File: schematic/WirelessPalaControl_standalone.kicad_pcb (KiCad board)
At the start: 2 copper layers, 25.6 x 34.3 mm, 25 parts, among them J1 6P4C, J2 MCU UART, J3 WeMos_mini_Hat_Left, J4 WeMos_mini_Hat_Right, Q1 AO3400A, Q2 AO3400A, U1 AMS1117-3.3

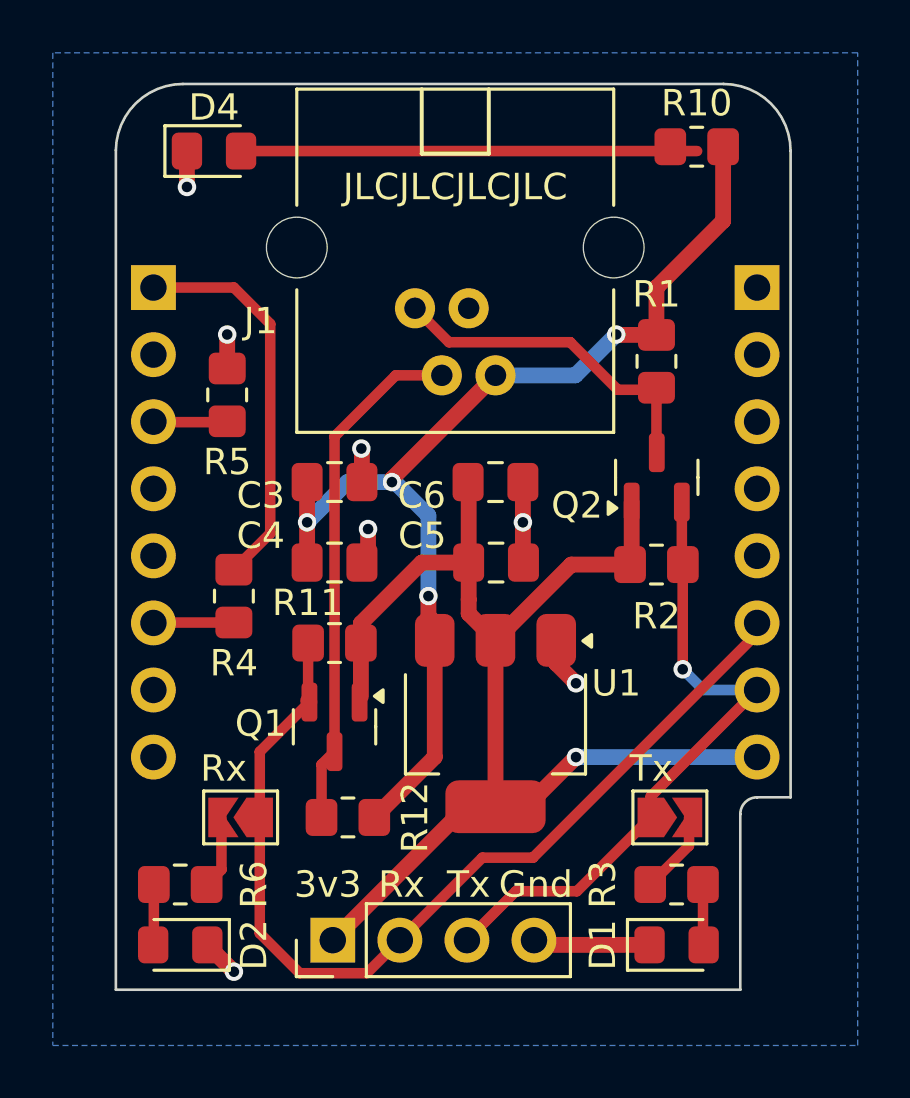
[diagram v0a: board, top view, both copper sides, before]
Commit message: feat(hw): Redesign standalone version with optionnal LED activation
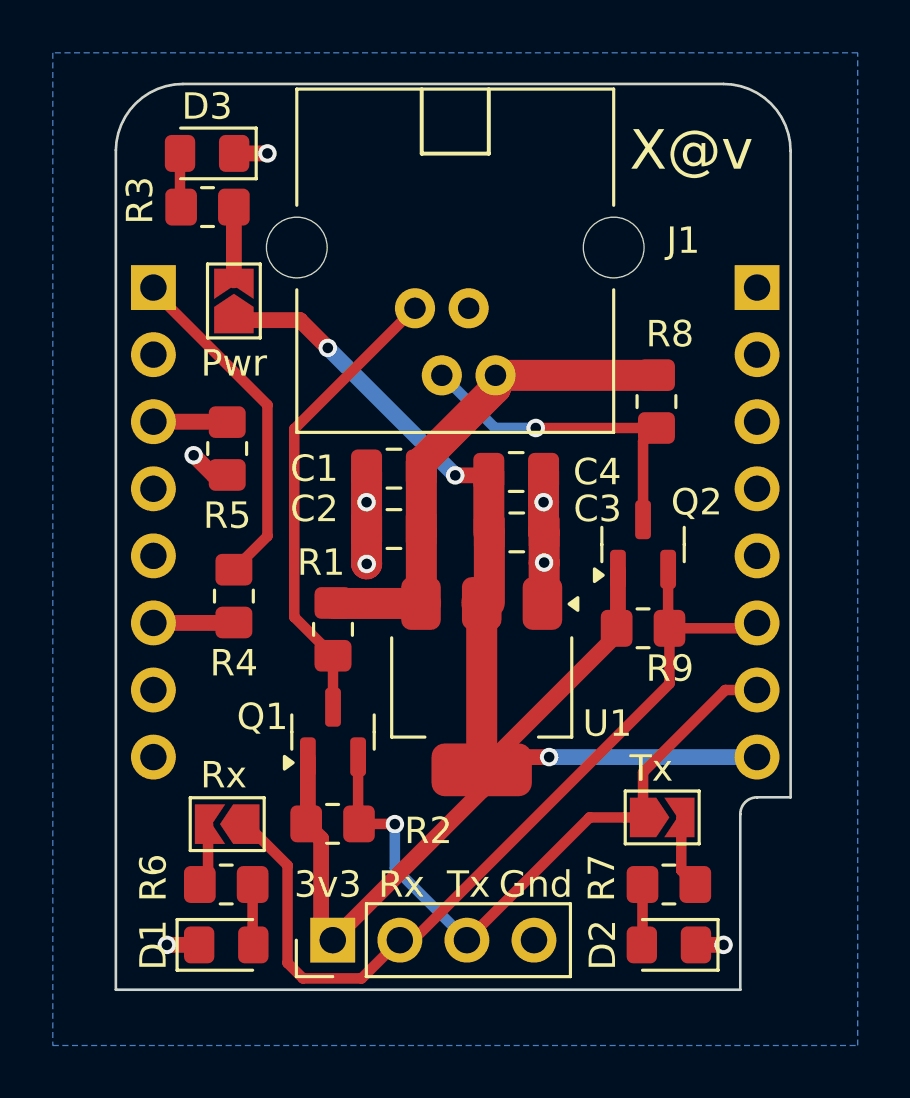
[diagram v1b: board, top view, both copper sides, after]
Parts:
- added JP3: SolderJumper_2_Open, Jumper:SolderJumper-2_P1.3mm_Open_TrianglePad1.0x1.5mm, F.Cu at (27.2, 32.3)
- moved R8 19.6 mm to (43.2, 36.1), turned to 90 degrees
- moved R3 18.7 mm to (26.2, 28.7)
- moved R1 15.9 mm to (30.9, 44.7)
- moved R2 15.7 mm to (30.9, 52.1)
- moved Q1 15.6 mm to (30.9, 48.6)
- moved Q2 13.6 mm to (42.7, 41.5), turned to 90 degrees
- moved R9 11.7 mm to (42.7, 44.7), turned to 180 degrees
- moved C2 2.58 mm to (33.2, 40.9), turned to 180 degrees
- moved C1 2.31 mm to (33.2, 38.6), turned to 180 degrees
- moved R5 2.03 mm to (26.9, 37.8), turned to -90 degrees
- moved D1 1.74 mm to (26.9, 56.6), turned to 0 degrees
- moved R6 1.74 mm to (26.9, 54.4), turned to 180 degrees
- moved U1 1.49 mm to (36.6, 46.9)
- moved C3 1.39 mm to (37.9, 41.0)
- moved C4 0.87 mm to (37.9, 38.7)
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- renumbered C3 to C1, C4 to C2, C5 to C3, C6 to C4, D2 to D1, D1 to D2, D4 to D3, Q2 to Q1, Q1 to Q2, R10 to R3, R3 to R7, R12 to R8, R11 to R9
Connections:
- R3 pad 2: +5V -> Net-(JP3-B)
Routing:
- net +5V: track 41.4 -> 19.3 mm, vias 4 -> 0
- net Net-(D3-A): track 17.3 -> 2.05 mm
- net +3.3V: track 48.7 -> 59.7 mm, vias 1 -> 3
- net Rx: track 19.7 -> 12.6 mm, vias 0 -> 1
- net Tx: track 12.9 -> 17.6 mm
- net RXuC: track 37.0 -> 33.0 mm
- net GND: track 16.8 -> 13.5 mm, vias 7 -> 8
- net Net-(JP3-B): track 0.00 -> 2.78 mm
- net /GPIO1: track 14.9 -> 13.0 mm
- net TXuC: track 24.9 -> 25.8 mm
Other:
- board text added: "Domochip WPalaControl V3.1"
- board text added: "Pwr"
- board text added: "X@v"
- board text removed: "Domochip WPalaControl V3.0"

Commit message: feat(hw): Add connector to directly solder a RJ11 cable
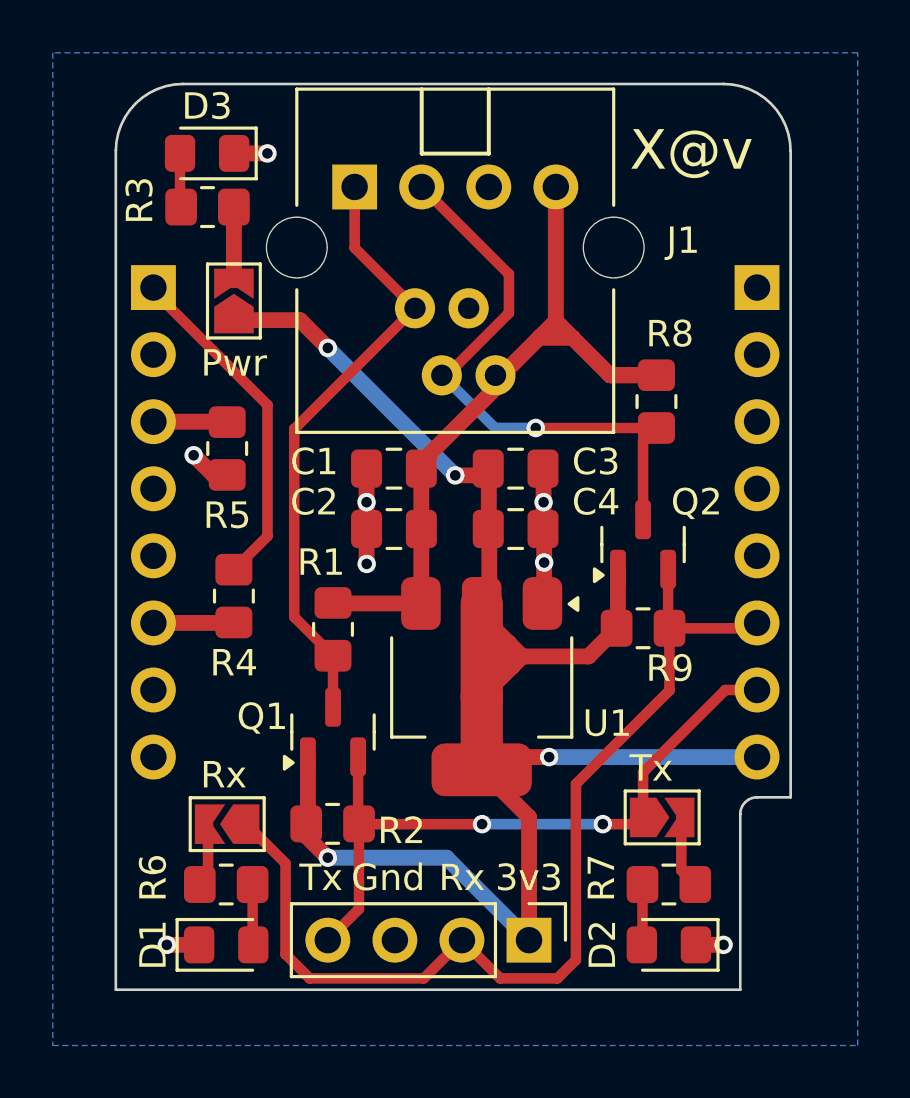
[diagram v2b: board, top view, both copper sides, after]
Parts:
- added J5: RJ11 - Direct Link, Connector_PinHeader_2.54mm:PinHeader_1x04_P2.54mm_Vertical, B.Cu at (31.8, 27.9)
- R1, R2, R8, R9: value 1K -> 10K
- moved J2 7.43 mm to (38.4, 56.5), turned to -90 degrees
- moved C3 2.41 mm to (37.8, 38.6)
- moved C4 2.16 mm to (37.8, 40.9)
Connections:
- J2 pad 3: TXuC -> GND
- J2 pad 4: GND -> TXuC
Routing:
- net +5V: track 19.3 -> 29.1 mm
- net Rx: track 12.6 -> 22.3 mm
- net +3.3V: track 59.7 -> 66.4 mm, vias 3 -> 4
- net Tx: track 17.6 -> 23.2 mm
- net RXuC: track 33.0 -> 38.1 mm
- net TXuC: vias 1 -> 2
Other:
- board text added: "RJ11 Y G R Bk colors"

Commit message: feat(hw): Update BOM with JLCPCB part numbers
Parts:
- R4: value 2K -> 1K
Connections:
- R4 pad 1: /GPIO1 -> /GPIO2
- R4 pad 2: /GPIO2 -> /GPIO1
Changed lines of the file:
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@@
 			)
 		)
-		(property "LCSC" "C17513"
+		(property "LCSC" "C17414"
 			(at 0 0 180)
 			(unlocked yes)
@@
 			)
 		)
-		(property "LCSC" "C17513"
+		(property "LCSC" "C17414"
 			(at 0 0 90)
 			(unlocked yes)
@@
 			)
 		)
-		(property "LCSC" "C84256"
+		(property "LCSC" "C2297"
 			(at 0 0 0)
 			(unlocked yes)
@@
 			)
 		)
-		(property "Value" "2K"
+		(property "Value" "1K"
 			(at 0 1.65 90)
 			(layer "F.Fab")
@@
 			)
 		)
-		(property "LCSC" "C17604"
+		(property "LCSC" "C17513"
 			(at 0 0 270)
 			(unlocked yes)
@@
 			(layers "F.Cu" "F.Mask" "F.Paste")
 			(roundrect_rratio 0.208333)
-			(net 8 "/GPIO1")
+			(net 12 "/GPIO2")
 			(pintype "passive")
 		)
@@
 			(layers "F.Cu" "F.Mask" "F.Paste")
 			(roundrect_rratio 0.208333)
-			(net 12 "/GPIO2")
+			(net 8 "/GPIO1")
 			(pintype "passive")
 		)
@@
 			)
 		)
-		(property "LCSC" "C17513"
+		(property "LCSC" "C17414"
 			(at 0 0 180)
 			(unlocked yes)
@@
 			)
 		)
-		(property "LCSC" "C17513"
+		(property "LCSC" "C17414"
 			(at 0 0 90)
 			(unlocked yes)
@@
 		(sheetname "/")
 		(sheetfile "WirelessPalaControl_standalone.kicad_sch")
-		(attr through_hole exclude_from_pos_files)
+		(attr through_hole exclude_from_pos_files exclude_from_bom)
 		(fp_line
 			(start 1.33 1.33)
@@
 		(sheetname "/")
 		(sheetfile "WirelessPalaControl_standalone.kicad_sch")
-		(attr through_hole exclude_from_pos_files)
+		(attr through_hole exclude_from_pos_files exclude_from_bom)
 		(fp_line
 			(start 1.33 -1.27)

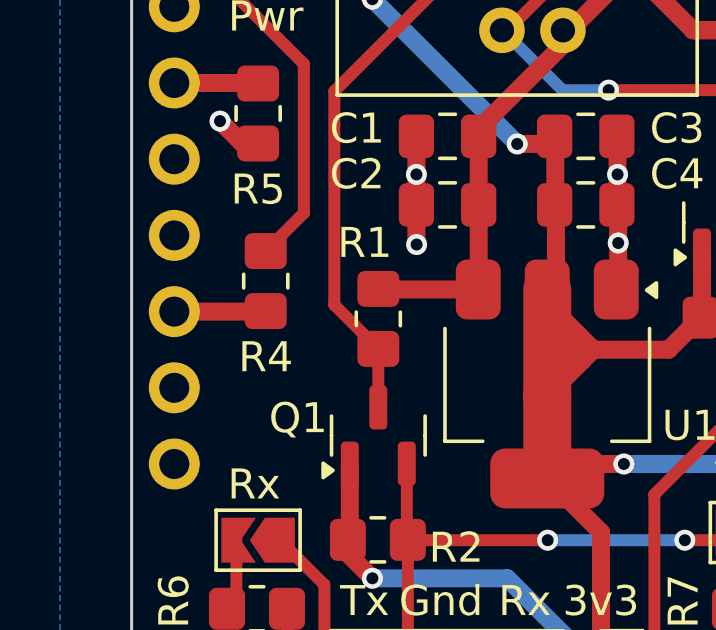
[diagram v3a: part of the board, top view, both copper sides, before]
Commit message: feat(hw): Cleanup schematic
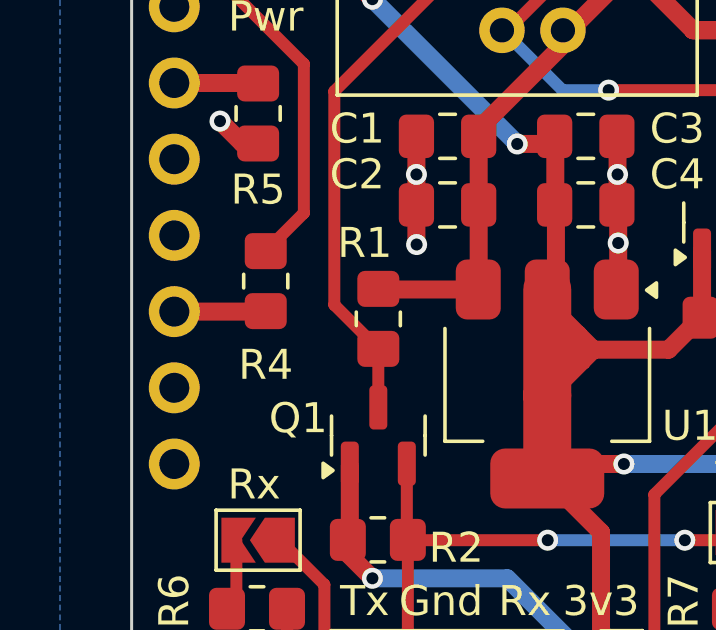
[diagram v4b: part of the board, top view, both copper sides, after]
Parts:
- turned R4 to 90 degrees
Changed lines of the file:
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@@
 	(footprint "Resistor_SMD:R_0805_2012Metric_Pad1.20x1.40mm_HandSolder"
 		(layer "F.Cu")
-		(at 27.178 43.434 -90)
+		(at 27.178 43.434 90)
 		(descr "Resistor SMD 0805 (2012 Metric), square (rectangular) end terminal, IPC_7351 nominal with elongated pad for handsoldering. (Body size source: IPC-SM-782 page 72, https://www.pcb-3d.com/wordpress/wp-content/uploads/ipc-sm-782a_amendment_1_and_2.pdf), generated with kicad-footprint-generator")
 		(tags "resistor handsolder")
 		(property "Reference" "R4"
-			(at 2.54 0 180)
+			(at -2.794 0 0)
 			(layer "F.SilkS")
 			(effects
@@
 		)
 		(property "Datasheet" "~"
-			(at 0 0 270)
+			(at 0 0 90)
 			(unlocked yes)
 			(layer "F.Fab")
@@
 		)
 		(property "Description" ""
-			(at 0 0 270)
+			(at 0 0 90)
 			(unlocked yes)
 			(layer "F.Fab")
@@
 		)
 		(property "LCSC" "C17513"
-			(at 0 0 270)
+			(at 0 0 90)
 			(unlocked yes)
 			(layer "F.Fab")
@@
 		(attr smd)
 		(fp_line
+			(start -0.227064 -0.735)
+			(end 0.227064 -0.735)
+			(stroke
+				(width 0.12)
+				(type solid)
+			)
+			(layer "F.SilkS")
+		)
+		(fp_line
 			(start -0.227064 0.735)
 			(end 0.227064 0.735)
@@
 		)
 		(fp_line
-			(start -0.227064 -0.735)
-			(end 0.227064 -0.735)
+			(start 1.85 -0.95)
+			(end 1.85 0.95)
 			(stroke
-				(width 0.12)
+				(width 0.05)
 				(type solid)
 			)
-			(layer "F.SilkS")
+			(layer "F.CrtYd")
 		)
 		(fp_line
-			(start -1.85 0.95)
-			(end -1.85 -0.95)
+			(start -1.85 -0.95)
+			(end 1.85 -0.95)
 			(stroke
 				(width 0.05)
@@
 		)
 		(fp_line
-			(start -1.85 -0.95)
-			(end 1.85 -0.95)
+			(start -1.85 0.95)
+			(end -1.85 -0.95)
 			(stroke
 				(width 0.05)
@@
 		)
 		(fp_line
-			(start 1.85 -0.95)
-			(end 1.85 0.95)
+			(start 1 -0.625)
+			(end 1 0.625)
 			(stroke
-				(width 0.05)
+				(width 0.1)
 				(type solid)
 			)
-			(layer "F.CrtYd")
+			(layer "F.Fab")
 		)
 		(fp_line
-			(start -1 0.625)
-			(end -1 -0.625)
+			(start -1 -0.625)
+			(end 1 -0.625)
 			(stroke
 				(width 0.1)
@@
 		)
 		(fp_line
-			(start -1 -0.625)
-			(end 1 -0.625)
-			(stroke
-				(width 0.1)
-				(type solid)
-			)
-			(layer "F.Fab")
-		)
-		(fp_line
-			(start 1 -0.625)
-			(end 1 0.625)
+			(start -1 0.625)
+			(end -1 -0.625)
 			(stroke
 				(width 0.1)
@@
 		)
 		(pad "1" smd roundrect
-			(at -1 0 270)
+			(at -1 0 90)
 			(size 1.2 1.4)
 			(layers "F.Cu" "F.Mask" "F.Paste")
@@
 		)
 		(pad "2" smd roundrect
-			(at 1 0 270)
+			(at 1 0 90)
 			(size 1.2 1.4)
 			(layers "F.Cu" "F.Mask" "F.Paste")

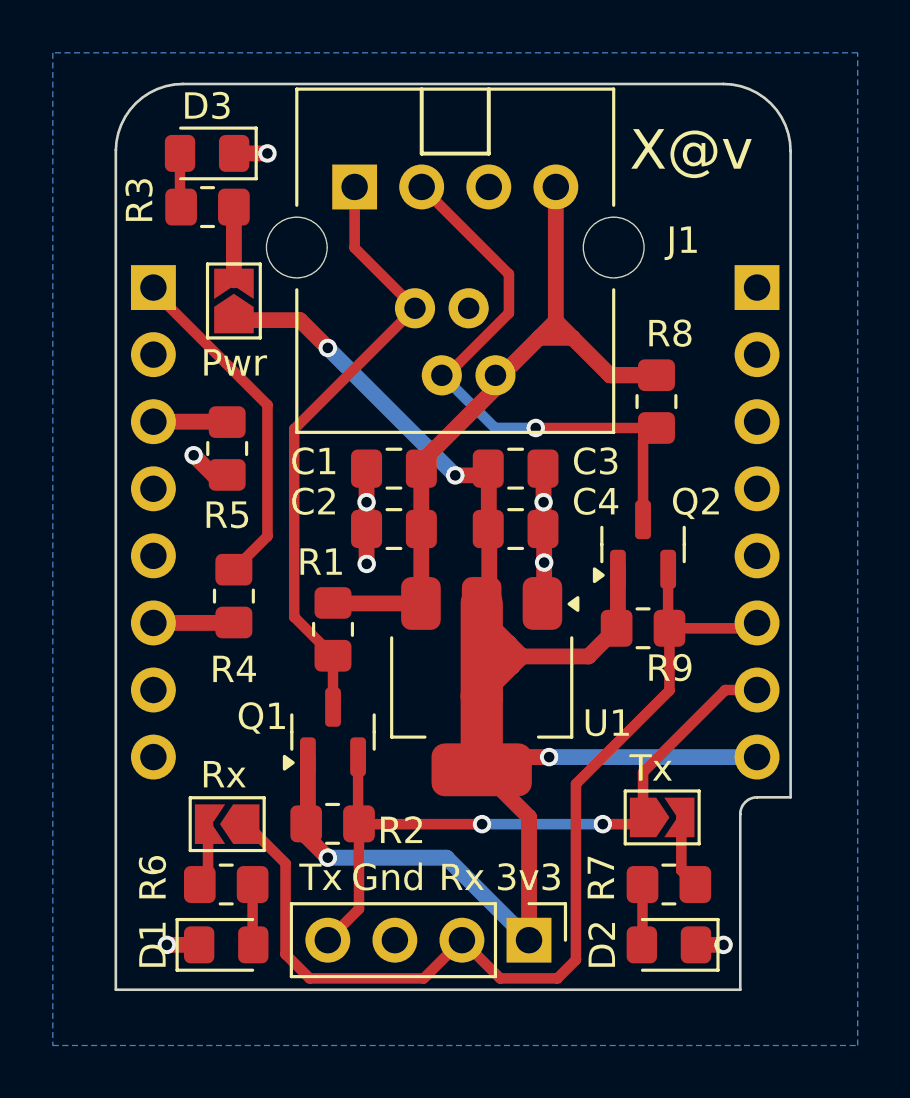
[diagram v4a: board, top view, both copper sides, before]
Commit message: feat(hw): cleanup PCB
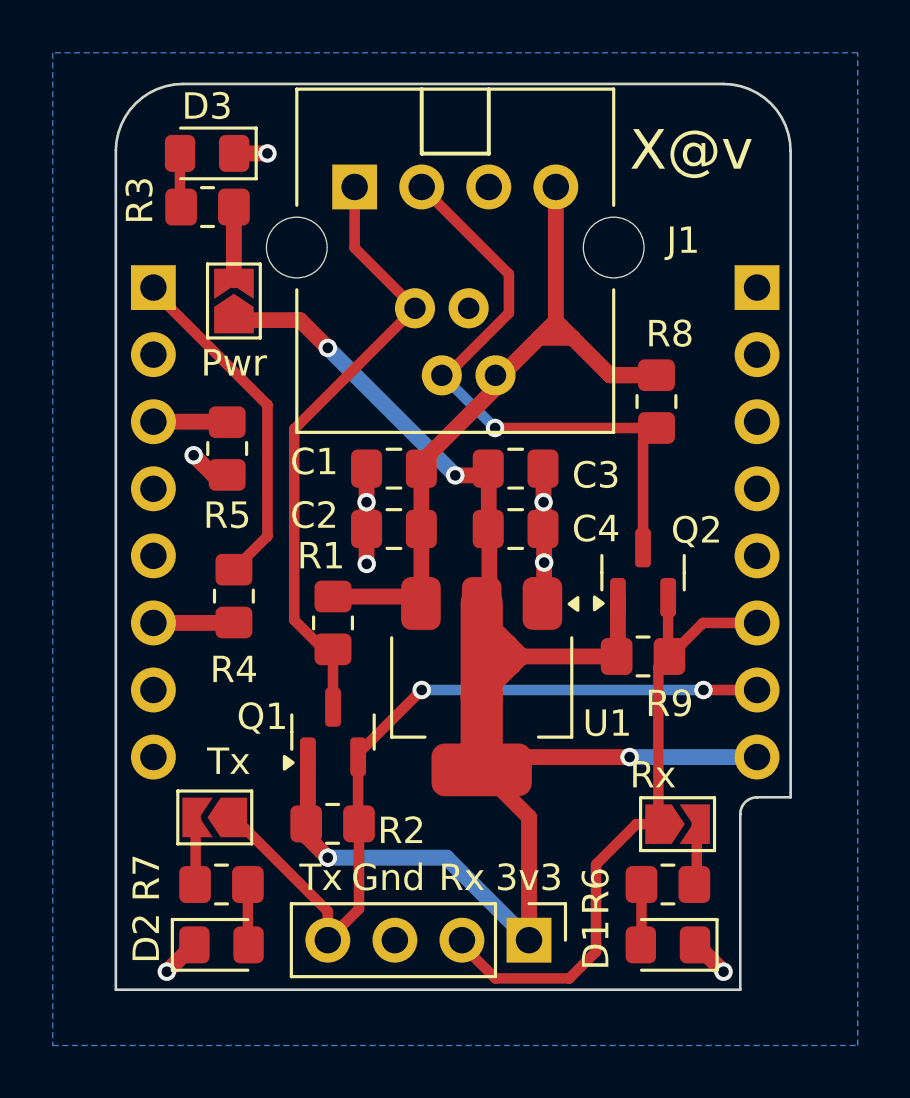
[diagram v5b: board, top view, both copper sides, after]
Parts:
- moved JP1 17.1 mm to (44.0, 52.1), turned to 0 degrees
- moved D2 16.9 mm to (26.7, 56.6), turned to 0 degrees
- moved R7 16.9 mm to (26.7, 54.4), turned to 180 degrees
- moved JP2 16.9 mm to (26.5, 51.8), turned to 180 degrees
- moved D1 16.7 mm to (43.6, 56.6), turned to 180 degrees
- moved R6 16.7 mm to (43.6, 54.4), turned to 0 degrees
- moved Q2 1.07 mm to (42.7, 42.5)
- moved R9 1.07 mm to (42.7, 45.7)
- moved R1 0.24 mm to (30.9, 44.5)
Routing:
- net RXuC: track 38.1 -> 25.1 mm
- net TXuC: track 25.8 -> 29.9 mm
- net Rx: track 22.3 -> 23.4 mm
- net +3.3V: track 66.4 -> 65.5 mm
- net GND: track 13.5 -> 14.2 mm
